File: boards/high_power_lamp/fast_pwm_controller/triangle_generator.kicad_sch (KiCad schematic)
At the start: 21 parts, among them U3 SPX5205-adjustable

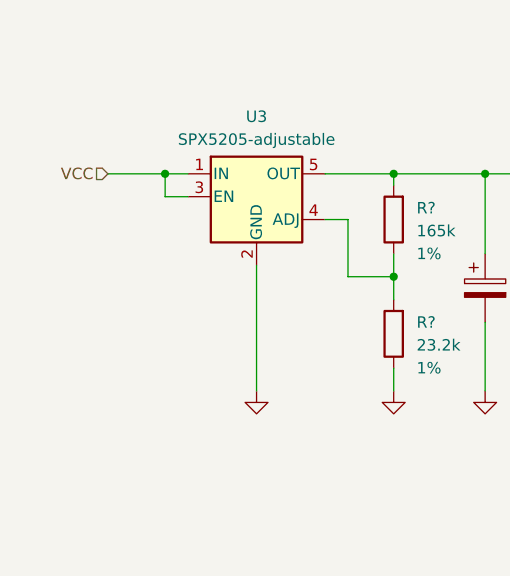
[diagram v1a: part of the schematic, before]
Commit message: almost finish arranging the fast pwm controller pcb
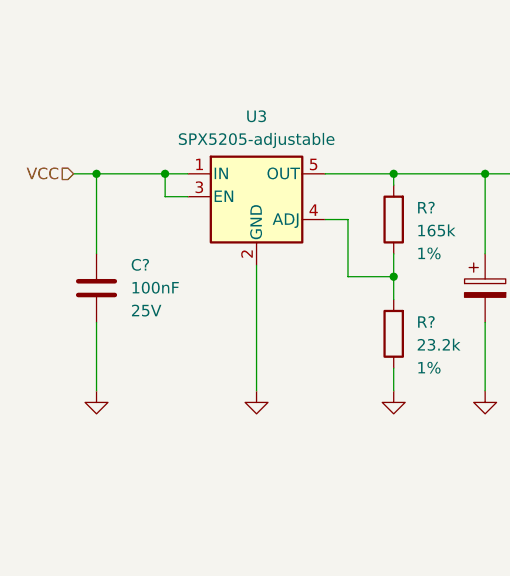
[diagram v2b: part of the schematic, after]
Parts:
- added C?: 100nF, Capacitor_SMD:C_0805_2012Metric, symbol Device:C
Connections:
- net GND: now also C?.1
- net VCC: now also C?.2
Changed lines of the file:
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@@
   (junction (at 243.84 44.45) (diameter 0) (color 0 0 0 0)
   )
+  (junction (at 39.37 78.74) (diameter 0) (color 0 0 0 0)
+  )
   (junction (at 165.1 110.49) (diameter 0) (color 0 0 0 0)
   )
@@
     (stroke (width 0) (type default))
   )
-  (wire (pts (xy 40.64 78.74) (xy 46.99 78.74))
+  (wire (pts (xy 36.83 78.74) (xy 39.37 78.74))
     (stroke (width 0) (type default))
   )
@@
     (stroke (width 0) (type default))
   )
+  (wire (pts (xy 39.37 78.74) (xy 46.99 78.74))
+    (stroke (width 0) (type default))
+  )
   (wire (pts (xy 243.84 85.09) (xy 243.84 73.66))
     (stroke (width 0) (type default))
@@
     (stroke (width 0) (type default))
   )
+  (wire (pts (xy 39.37 78.74) (xy 39.37 87.63))
+    (stroke (width 0) (type default))
+  )
   (wire (pts (xy 177.8 110.49) (xy 180.34 110.49))
     (stroke (width 0) (type default))
@@
   )
   (wire (pts (xy 72.39 90.17) (xy 72.39 92.71))
+    (stroke (width 0) (type default))
+  )
+  (wire (pts (xy 39.37 95.25) (xy 39.37 102.87))
     (stroke (width 0) (type default))
   )
@@
     (effects (font (size 1.27 1.27)) (justify left bottom))
   )
-  (hierarchical_label "VCC" (shape input) (at 40.64 78.74 180) (fields_autoplaced)
+  (hierarchical_label "VCC" (shape input) (at 36.83 78.74 180) (fields_autoplaced)
     (effects (font (size 1.27 1.27)) (justify right))
   )
@@
         )
       )
+    )
+  )
+  (symbol (lib_id "power:GND") (at 39.37 102.87 0) (unit 1)
+    (in_bom yes) (on_board yes) (dnp no) (fields_autoplaced)
+    (property "Reference" "#PWR04" (at 39.37 109.22 0)
+      (effects (font (size 1.27 1.27)) hide)
+    )
+    (property "Value" "GND" (at 39.37 107.95 0)
+      (effects (font (size 1.27 1.27)) hide)
+    )
+    (property "Footprint" "" (at 39.37 102.87 0)
+      (effects (font (size 1.27 1.27)) hide)
+    )
+    (property "Datasheet" "" (at 39.37 102.87 0)
+      (effects (font (size 1.27 1.27)) hide)
+    )
+    (pin "1")
+    (instances
+      (project "fast_pwm_controller"
+        (path "/ebb02bb0-15d4-41b5-b7b0-053d51d38d86"
+          (reference "#PWR04") (unit 1)
+        )
+        (path "/ebb02bb0-15d4-41b5-b7b0-053d51d38d86/e05c2491-0151-410f-b890-9105113d0b96"
+          (reference "#PWR056") (unit 1)
+        )
+      )
+    )
+  )
+  (symbol (lib_id "Device:C") (at 39.37 91.44 180) (unit 1)
+    (in_bom yes) (on_board yes) (dnp no)
+    (property "Reference" "C?" (at 43.18 88.9 0)
+      (effects (font (size 1.27 1.27)) (justify right))
+    )
+    (property "Value" "100nF" (at 43.18 91.44 0)
+      (effects (font (size 1.27 1.27)) (justify right))
+    )
+    (property "Footprint" "Capacitor_SMD:C_0805_2012Metric" (at 38.4048 87.63 0)
+      (effects (font (size 1.27 1.27)) hide)
+    )
+    (property "Datasheet" "~" (at 39.37 91.44 0)
+      (effects (font (size 1.27 1.27)) hide)
+    )
+    (property "Info" "25V" (at 43.18 93.98 0)
+      (effects (font (size 1.27 1.27)) (justify right))
+    )
+    (pin "1")
+    (pin "2")
+    (instances
+      (project "fast_pwm_controller"
+        (path "/ebb02bb0-15d4-41b5-b7b0-053d51d38d86"
+          (reference "C?") (unit 1)
+        )
+        (path "/ebb02bb0-15d4-41b5-b7b0-053d51d38d86/e05c2491-0151-410f-b890-9105113d0b96"
+          (reference "C?") (unit 1)
+        )
+      )

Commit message: arrange everything
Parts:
- gave numbers to parts that had none: 17
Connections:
- net TRIANGLE: now also U4.13 (-), U4.14; no longer U4.8, U4.9 (-)
- net at C7.2, R6.1, R7.1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: now also U4.12 (+); no longer U4.10 (+)
